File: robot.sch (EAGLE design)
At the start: 8 parts

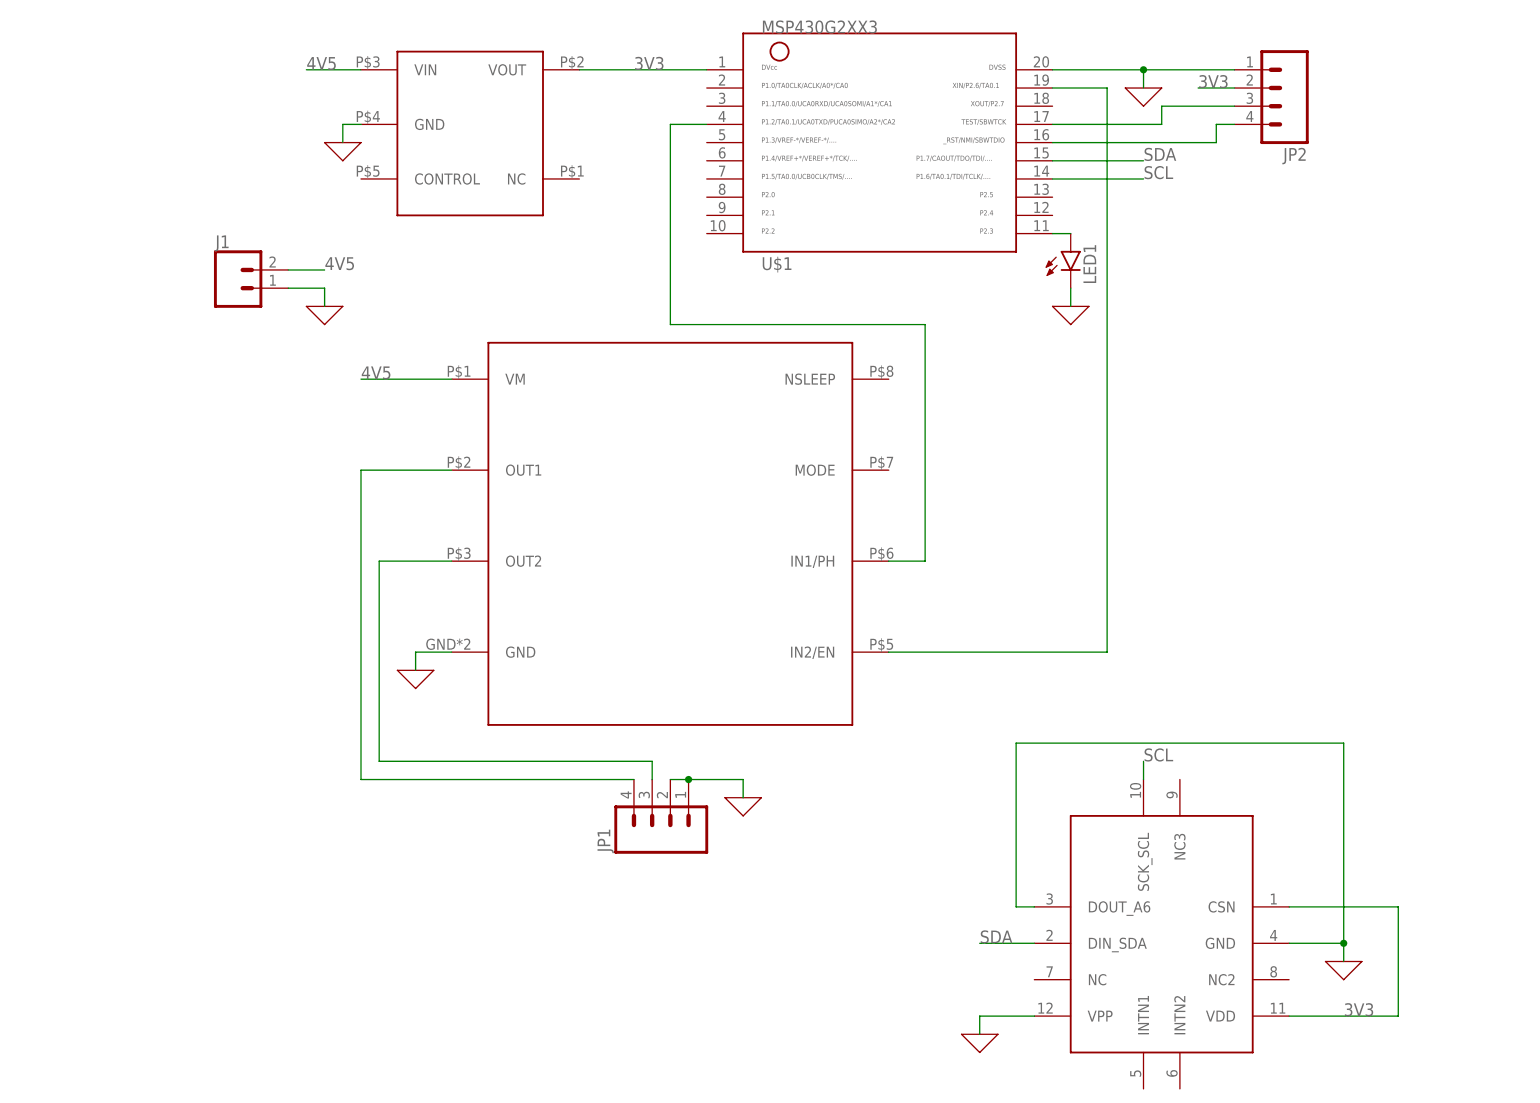
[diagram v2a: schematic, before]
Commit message: Schematic complete for review.
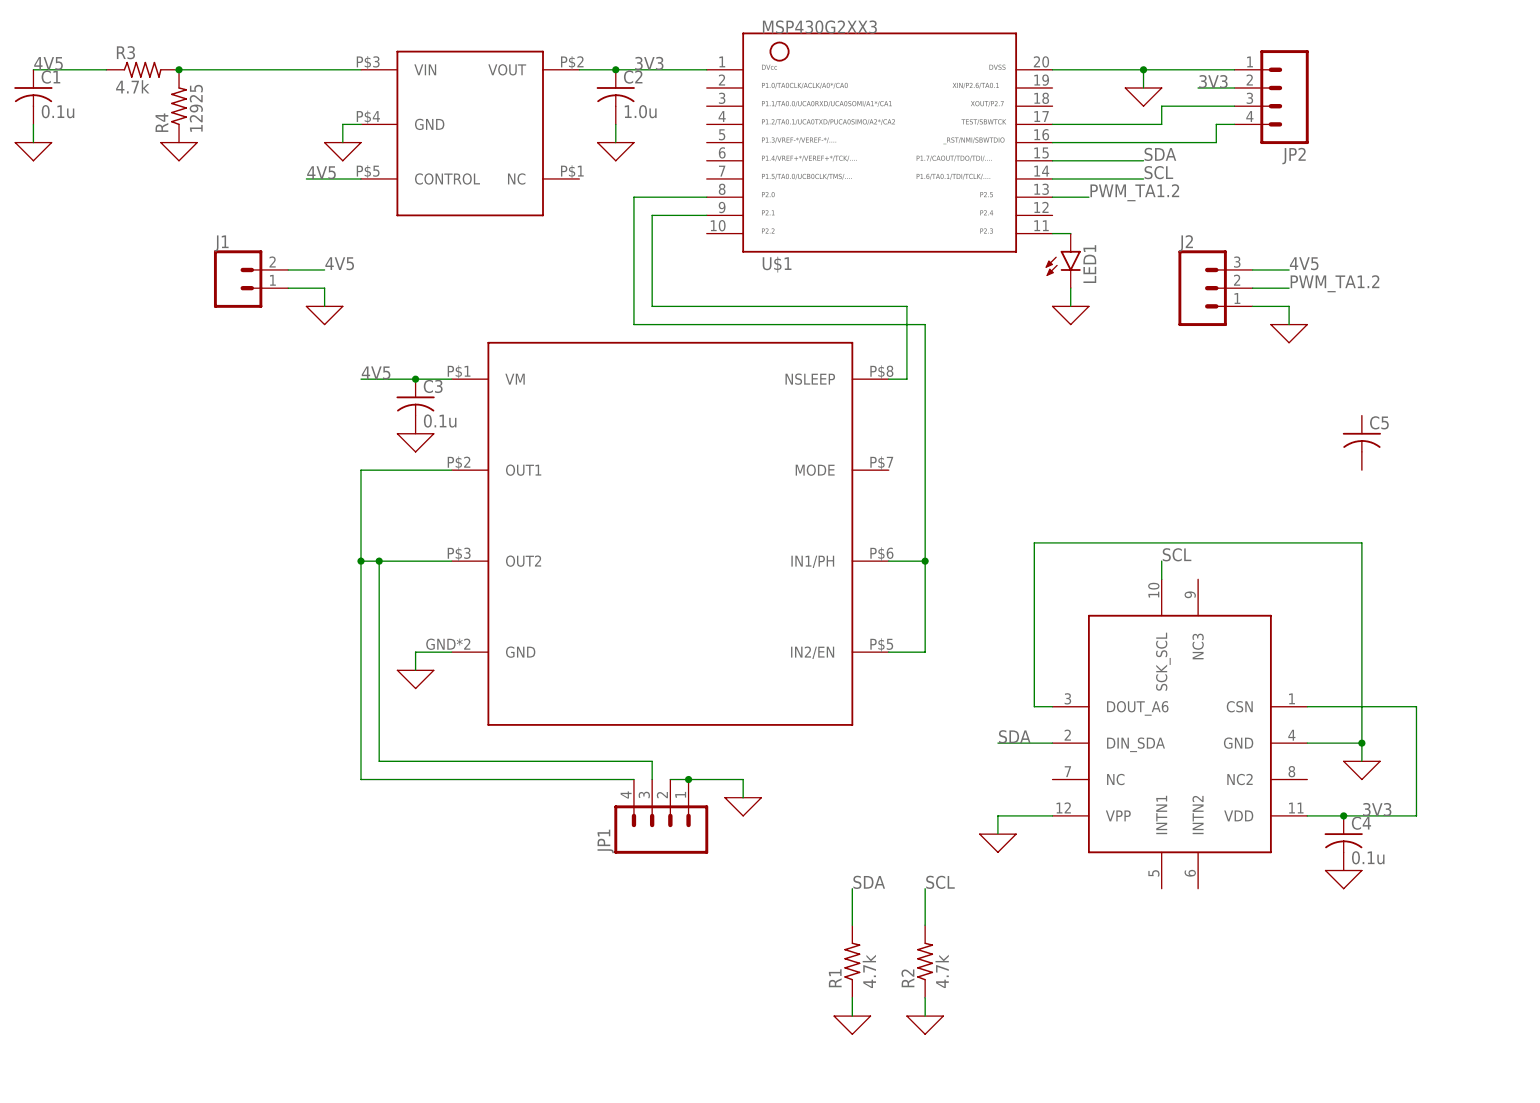
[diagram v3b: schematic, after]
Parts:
- added C1, C3, C4: 0.1u, rcl:C-USC0805
- added C2: 1.0u, rcl:C-USC0805
- added C5: (no value), rcl:C-USC0805
- added J2: (no value), SparkFun-Connectors:CONN_03LOCK
- added R1, R2, R3: 4.7k, rcl:R-US_R0805
- added R4: 12925, rcl:R-US_R0805
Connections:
- removed net N$9: JP1.4, U$2.OUT1
- new net N$2: U$1.9, U$2.NSLEEP
- new net PWM_TA1.2: J2.2, U$1.13
- net 0: now also C1.2, C2.2, C3.2, C4.2, J2.1, R1.1, R2.1, R4.1
- net 3V3: now also C2.1, C4.1
- net 4V5: now also C1.1, C3.1, J2.3, R3.1, U$4.CONTROL; no longer U$4.VIN
- net N$4: now also U$1.8, U$2.IN2/EN; no longer U$1.4
- net N$5: now also R3.2, R4.2, U$4.VIN; no longer U$1.19, U$2.IN2/EN
- net N$8: now also JP1.4, U$2.OUT1
- net SCL: now also R2.2
- net SDA: now also R1.2

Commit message: Added board
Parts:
- removed C5: (no value), rcl:C-USC0805
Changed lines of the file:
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@@
 <part name="C3" library="rcl" library_urn="urn:adsk.eagle:library:334" deviceset="C-US" device="C0805" package3d_urn="urn:adsk.eagle:package:23617/2" value="0.1u"/>
 <part name="C4" library="rcl" library_urn="urn:adsk.eagle:library:334" deviceset="C-US" device="C0805" package3d_urn="urn:adsk.eagle:package:23617/2" value="0.1u"/>
-<part name="C5" library="rcl" library_urn="urn:adsk.eagle:library:334" deviceset="C-US" device="C0805" package3d_urn="urn:adsk.eagle:package:23617/2"/>
 <part name="X_10" library="ngspice-simulation" library_urn="urn:adsk.eagle:library:527439" deviceset="GND" device=""/>
 <part name="X_11" library="ngspice-simulation" library_urn="urn:adsk.eagle:library:527439" deviceset="GND" device=""/>
@@
 <attribute name="VALUE" x="135.636" y="-39.751" size="1.778" layer="96"/>
 </instance>
-<instance part="C5" gate="G$1" x="137.16" y="20.32" smashed="yes">
-<attribute name="NAME" x="138.176" y="20.955" size="1.778" layer="95"/>
-<attribute name="VALUE" x="138.176" y="16.129" size="1.778" layer="96"/>
-</instance>
 <instance part="X_10" gate="G$1" x="-48.26" y="60.96" smashed="yes"/>

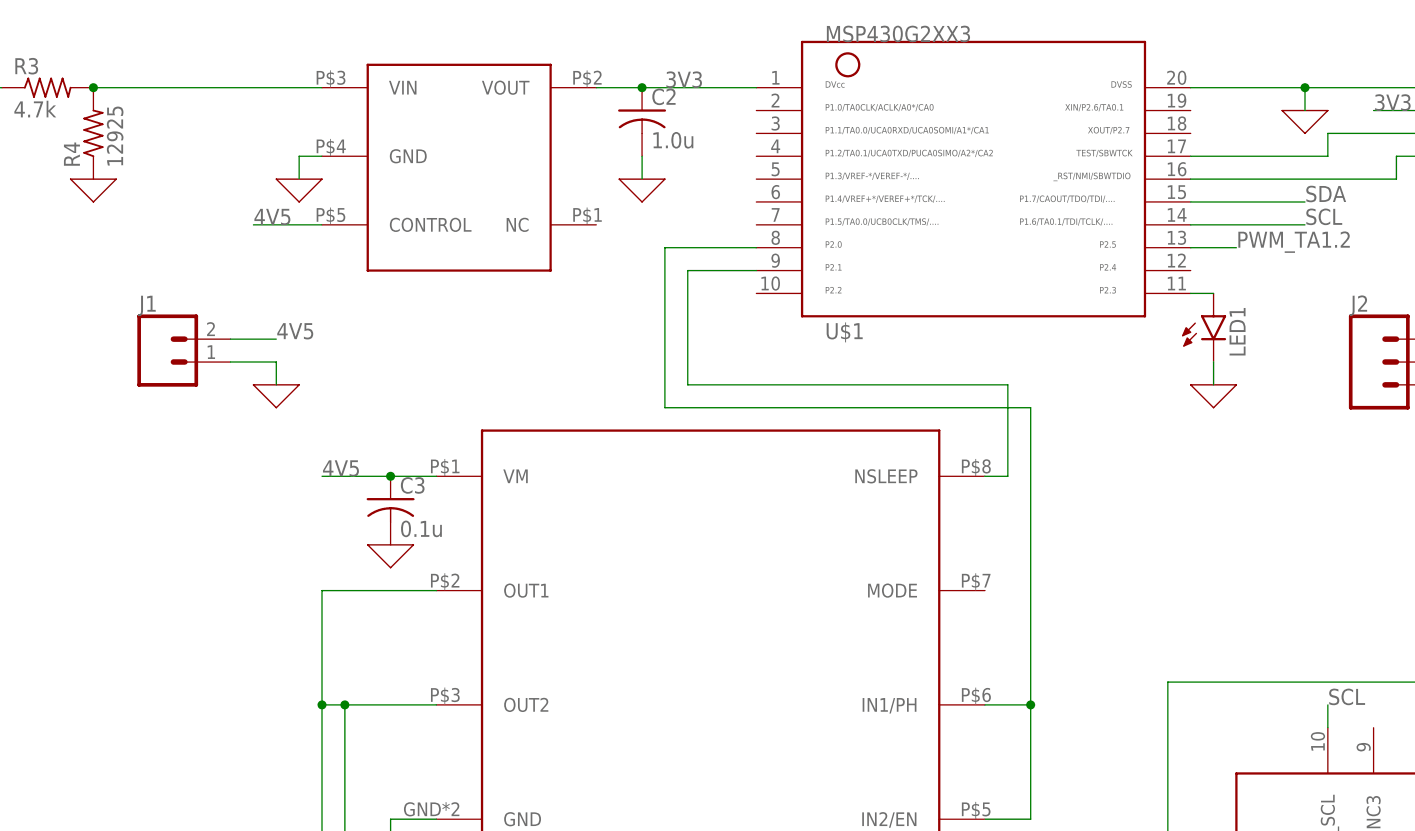
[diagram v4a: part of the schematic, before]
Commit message: Added power planes to board and also added a resistor for the LED.
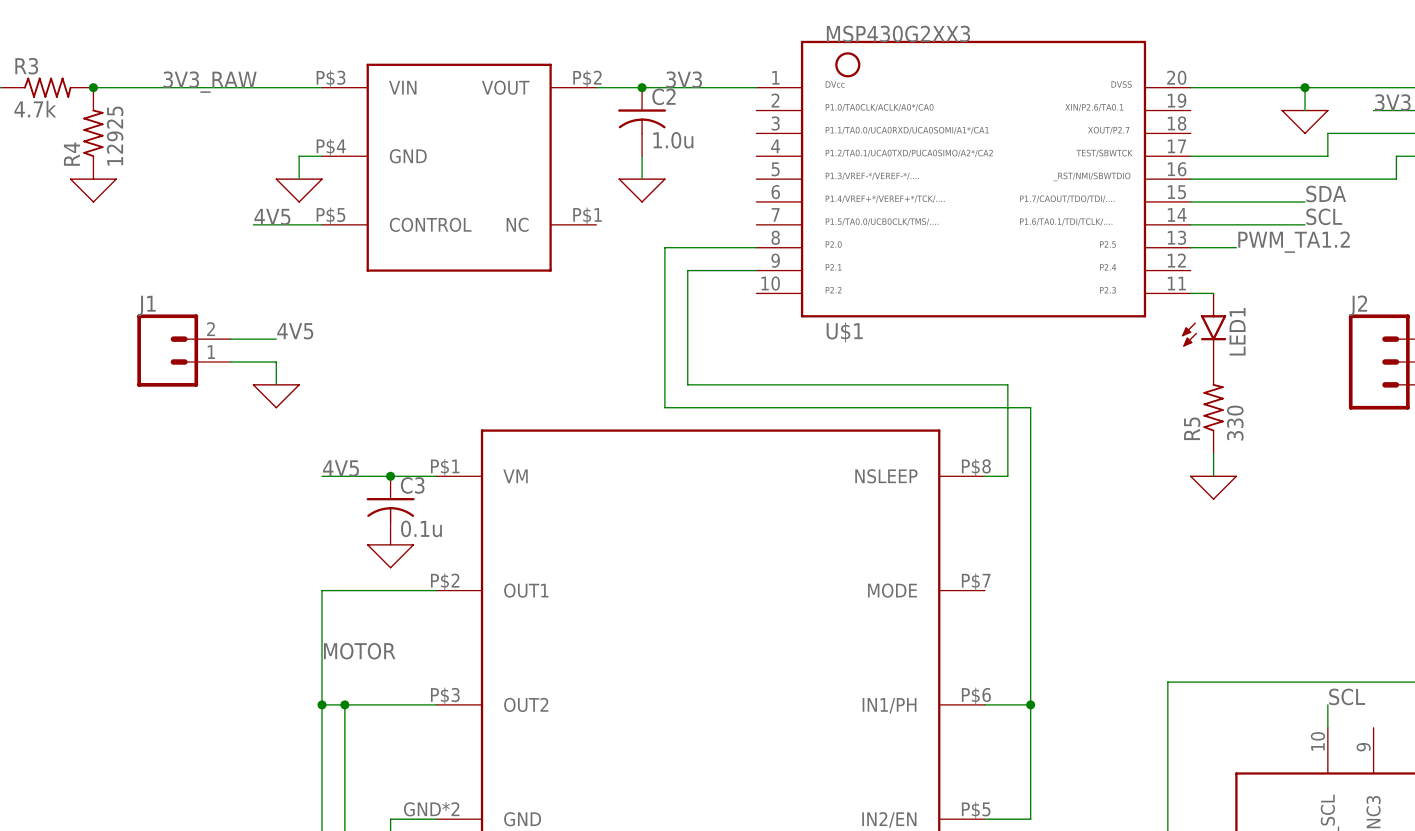
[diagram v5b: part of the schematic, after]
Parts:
- added R5: 330, rcl:R-US_R0805
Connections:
- net N$5 renamed 3V3_RAW
- net N$8 renamed MOTOR
- new net N$3: LED1.C, R5.2
- net 0: now also R5.1; no longer LED1.C
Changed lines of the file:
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@@
 <class number="0" name="default" width="0" drill="0">
+</class>
+<class number="1" name="New Class" width="0" drill="0">
 </class>
 </classes>
@@
 <part name="R4" library="rcl" library_urn="urn:adsk.eagle:library:334" deviceset="R-US_" device="R0805" package3d_urn="urn:adsk.eagle:package:23553/2" value="12925"/>
 <part name="X_16" library="ngspice-simulation" library_urn="urn:adsk.eagle:library:527439" deviceset="GND" device=""/>
+<part name="R5" library="rcl" library_urn="urn:adsk.eagle:library:334" deviceset="R-US_" device="R0805" package3d_urn="urn:adsk.eagle:package:23553/2" value="330"/>
 </parts>
 <sheets>
@@
 </instance>
 <instance part="X_7" gate="G$1" x="-7.62" y="38.1" smashed="yes"/>
-<instance part="X_8" gate="G$1" x="96.52" y="38.1" smashed="yes"/>
+<instance part="X_8" gate="G$1" x="96.52" y="27.94" smashed="yes"/>
 <instance part="X_4" gate="G$1" x="50.8" y="-30.48" smashed="yes"/>
 <instance part="J2" gate="J$1" x="114.3" y="40.64" smashed="yes">
@@
 </instance>
 <instance part="X_16" gate="G$1" x="-27.94" y="60.96" smashed="yes"/>
+<instance part="R5" gate="G$1" x="96.52" y="35.56" smashed="yes" rot="R90">
+<attribute name="NAME" x="95.0214" y="31.75" size="1.778" layer="95" rot="R90"/>
+<attribute name="VALUE" x="99.822" y="31.75" size="1.778" layer="96" rot="R90"/>
+</instance>
 </instances>
 <busses>
@@
 </segment>
 <segment>
-<pinref part="X_8" gate="G$1" pin="0"/>
-<pinref part="LED1" gate="G$1" pin="C"/>
-<wire x1="96.52" y1="38.1" x2="96.52" y2="40.64" width="0.1524" layer="91"/>
-</segment>
-<segment>
 <pinref part="JP1" gate="G$1" pin="1"/>
 <wire x1="43.18" y1="-27.94" x2="50.8" y2="-27.94" width="0.1524" layer="91"/>
@@
 <pinref part="X_16" gate="G$1" pin="0"/>
 <pinref part="R4" gate="G$1" pin="1"/>
+</segment>
+<segment>
+<pinref part="X_8" gate="G$1" pin="0"/>
+<pinref part="R5" gate="G$1" pin="1"/>
+<wire x1="96.52" y1="27.94" x2="96.52" y2="30.48" width="0.1524" layer="91"/>
 </segment>
 </net>
@@
 </segment>
 </net>
-<net name="N$8" class="0">
+<net name="MOTOR" class="0">
 <segment>
 <pinref part="U$2" gate="G$1" pin="OUT2"/>
@@
 <junction x="0" y="2.54"/>
 <junction x="-2.54" y="2.54"/>
+<label x="-2.54" y="7.62" size="1.778" layer="95"/>
 </segment>
 </net>
@@
 </segment>
 </net>
-<net name="N$5" class="0">
+<net name="3V3_RAW" class="0">
 <segment>
 <pinref part="R4" gate="G$1" pin="2"/>
@@
 <wire x1="-27.94" y1="71.12" x2="-2.54" y2="71.12" width="0.1524" layer="91"/>
 <junction x="-27.94" y="71.12"/>
-</segment>
-</net>
+<label x="-20.32" y="71.12" size="1.778" layer="95"/>
+</segment>
+</net>
+<net name="N$3" class="0">
+<segment>
+<pinref part="R5" gate="G$1" pin="2"/>
+<pinref part="LED1" gate="G$1" pin="C"/>
+</segment>
+</net>

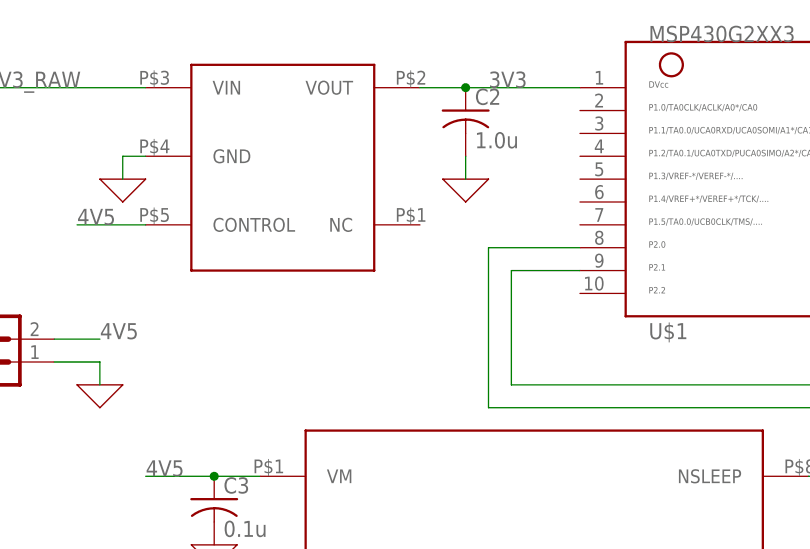
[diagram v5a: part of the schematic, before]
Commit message: Added two-pin header to board for interface with BeagleBone.
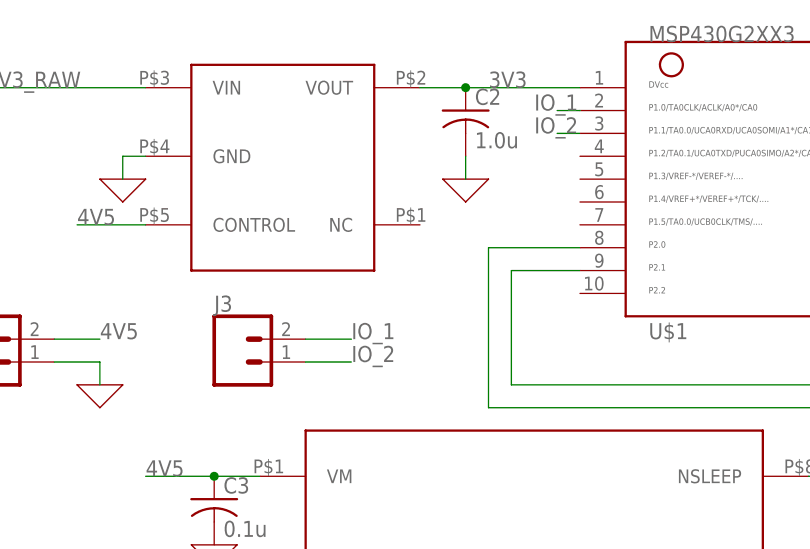
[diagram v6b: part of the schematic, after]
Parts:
- added J3: (no value), SparkFun-Connectors:CONN_02
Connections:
- new net IO_1: J3.2, U$1.2
- new net IO_2: J3.1, U$1.3
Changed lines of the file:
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@@
 <part name="X_16" library="ngspice-simulation" library_urn="urn:adsk.eagle:library:527439" deviceset="GND" device=""/>
 <part name="R5" library="rcl" library_urn="urn:adsk.eagle:library:334" deviceset="R-US_" device="R0805" package3d_urn="urn:adsk.eagle:package:23553/2" value="330"/>
+<part name="J3" library="SparkFun-Connectors" library_urn="urn:adsk.eagle:library:513" deviceset="CONN_02" device="" package3d_urn="urn:adsk.eagle:package:38039/1"/>
 </parts>
 <sheets>
@@
 <attribute name="NAME" x="95.0214" y="31.75" size="1.778" layer="95" rot="R90"/>
 <attribute name="VALUE" x="99.822" y="31.75" size="1.778" layer="96" rot="R90"/>
+</instance>
+<instance part="J3" gate="G$1" x="7.62" y="40.64" smashed="yes">
+<attribute name="VALUE" x="5.08" y="35.814" size="1.778" layer="96" font="vector"/>
+<attribute name="NAME" x="5.08" y="46.228" size="1.778" layer="95" font="vector"/>
 </instance>
 </instances>
@@
 </segment>
 </net>
+<net name="IO_1" class="0">
+<segment>
+<pinref part="U$1" gate="G$1" pin="2"/>
+<wire x1="45.72" y1="68.58" x2="43.18" y2="68.58" width="0.1524" layer="91"/>
+<label x="40.64" y="68.58" size="1.778" layer="95"/>
+</segment>
+<segment>
+<pinref part="J3" gate="G$1" pin="2"/>
+<wire x1="15.24" y1="43.18" x2="20.32" y2="43.18" width="0.1524" layer="91"/>
+<label x="20.32" y="43.18" size="1.778" layer="95"/>
+</segment>
+</net>
+<net name="IO_2" class="0">
+<segment>
+<pinref part="U$1" gate="G$1" pin="3"/>
+<wire x1="45.72" y1="66.04" x2="43.18" y2="66.04" width="0.1524" layer="91"/>
+<label x="40.64" y="66.04" size="1.778" layer="95"/>
+</segment>
+<segment>
+<pinref part="J3" gate="G$1" pin="1"/>
+<wire x1="15.24" y1="40.64" x2="20.32" y2="40.64" width="0.1524" layer="91"/>
+<label x="20.32" y="40.64" size="1.778" layer="95"/>
+</segment>
+</net>
